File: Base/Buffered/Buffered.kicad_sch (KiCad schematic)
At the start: 17 parts, among them J1 Barrel_Jack_Switch, J2 Conn_01x04_Pin, J3 Conn_01x04_Pin, J4 AudioJack2_Ground, J5 AudioJack2_Ground, Q2 40V, SW1 SW_Push

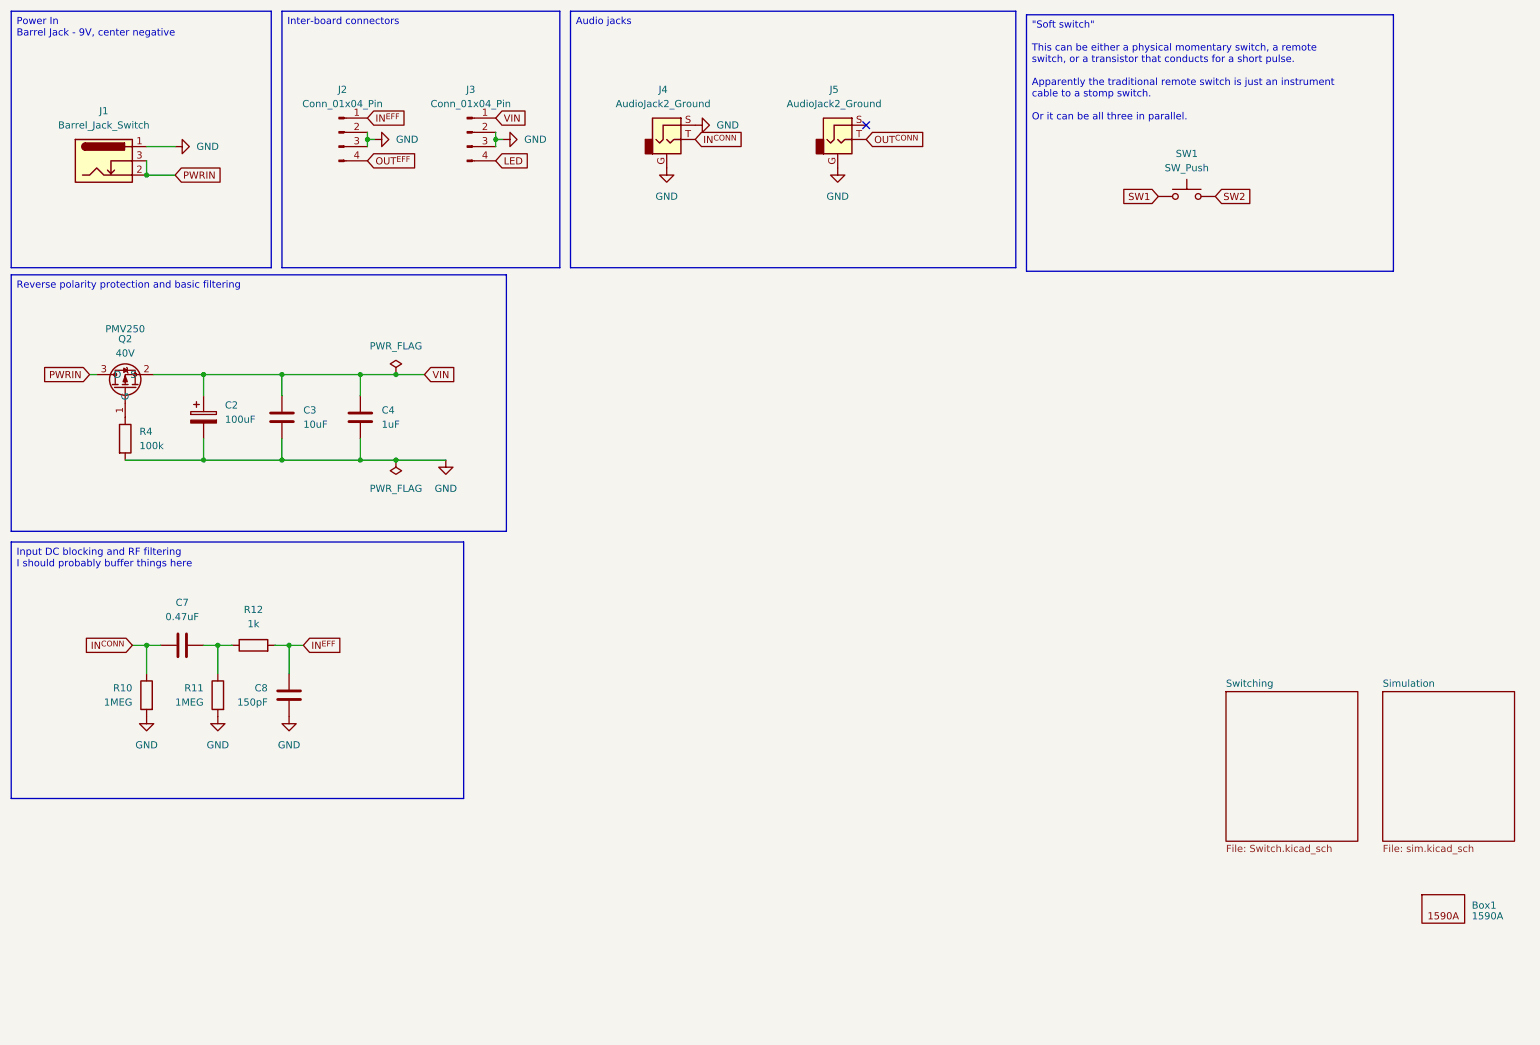
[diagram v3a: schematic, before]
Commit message: Add negative power rail to the buffered base design
The negative voltage isn't actually _used_ anywhere yet, but this is
prep-work for making that buffered base board do the long promised
buffering, as I'm currently leaning towards opamps.

The LT3462A is very easy to use, but in a probably completely misguided
attempt at keeping any stray ground return currents on the power supply
side, I added a ground plane keepout.  No isolation, but an attempt to
at least make the easy path for any return currents to stay in that
"power supply area" and hopefully not show up around the analog parts.

Somebody who knows what they are about would probably tell me I'm just
making things worse.  But I'm a sw engineer, so pretty much by
definition I don't know anybody who knows what they are doing.

Signed-off-by: Linus Torvalds <torvalds@linux-foundation.org>
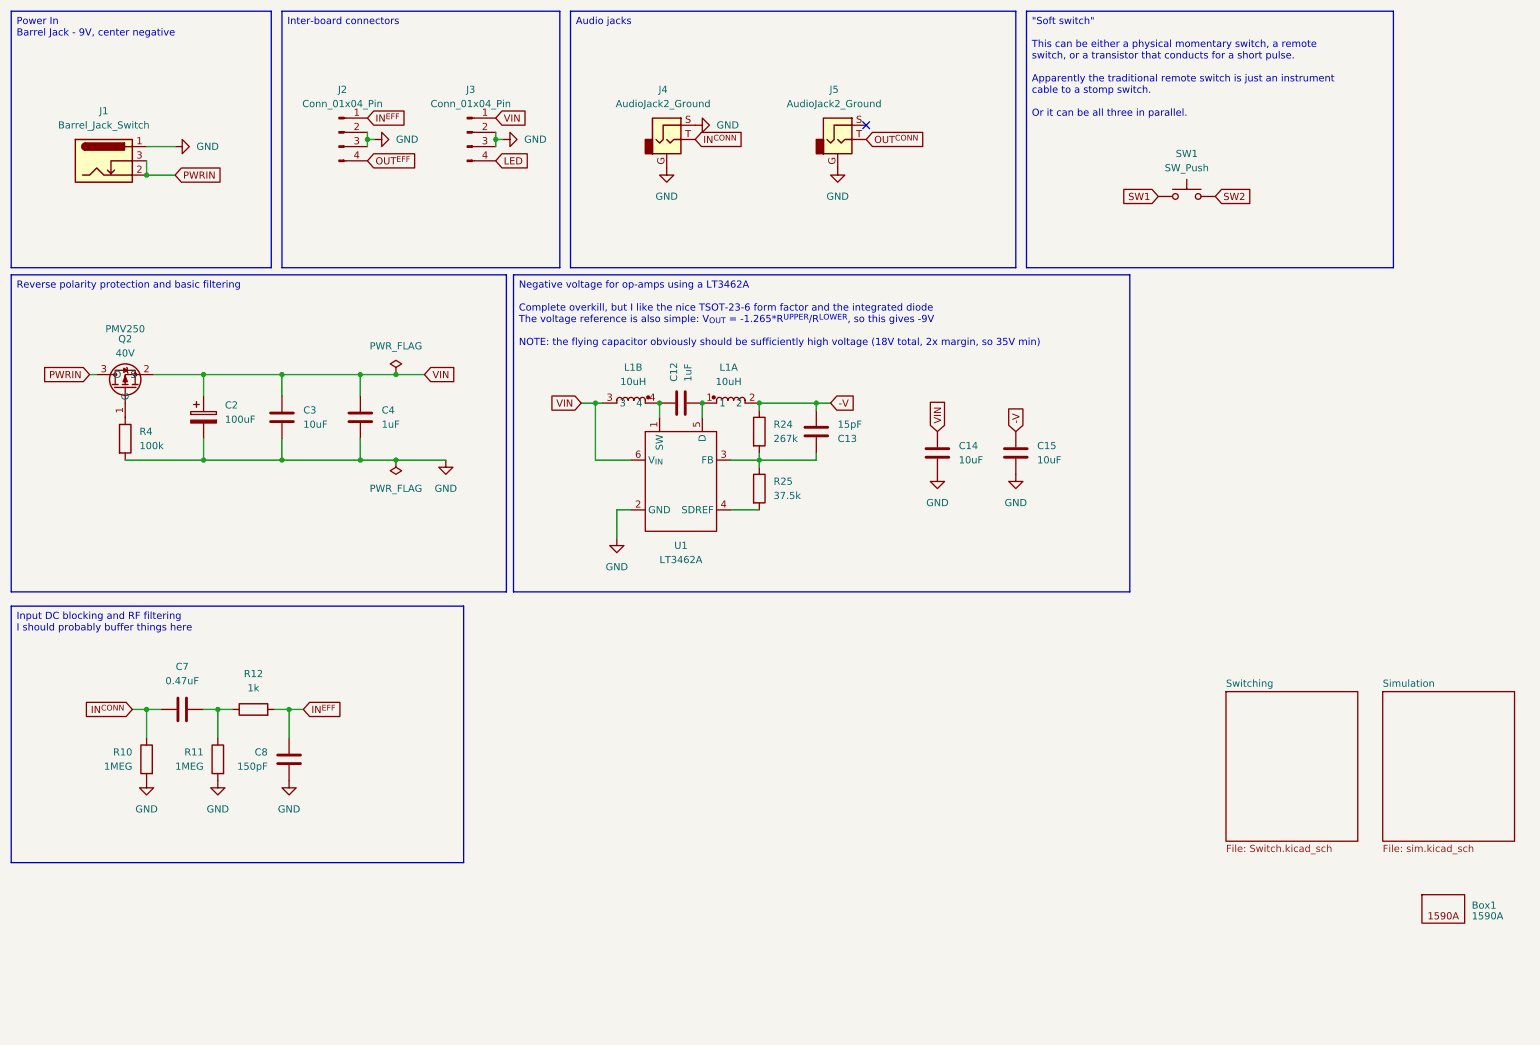
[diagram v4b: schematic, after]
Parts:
- added C12: 1uF, Capacitor_SMD:C_1206_3216Metric, symbol Device:C
- added C13: 15pF, Capacitor_SMD:C_0805_2012Metric, symbol Device:C
- added C14, C15: 10uF, Capacitor_SMD:C_1206_3216Metric, symbol Device:C
- added L1: 10uH, Mylib:LPD5030, symbol Mylib:LPD5030
- added R24: 267k, Resistor_SMD:R_0805_2012Metric, symbol Device:R
- added R25: 37.5k, Resistor_SMD:R_0805_2012Metric, symbol Device:R
- added U1: LT3462A, Package_TO_SOT_SMD:TSOT-23-6, symbol Mylib:LT3462AES6
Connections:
- net GND: now also C14.2, C15.2, U1.2 (GND)
- net VIN: now also C14.1, L1.3, U1.6 (V_{IN})
- new net: C12.2, L1.1, U1.5 (D)
- new net: C13.1, R24.2, R25.1, U1.3 (FB)
- new net: C12.1, L1.4, U1.1 (SW)
- new net: R25.2, U1.4 (SDREF)
- new net -V: C13.2, C15.1, L1.2, R24.1
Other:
- moved on the sheet: C7, C8, R10, R11, R12

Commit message: Buffered base: use negative rail for JFET switching
This _still_ doesn't do any actual buffering, but with the negative
rail, we now no longer need to rebase the signals to some mid-point
voltage, and we can just leave the signals ground-references and use the
negative rail for switching.

That streamlines the signal path, and will make it easier to just insert
an opamp or two in there too.  But I remain more interested in getting
the switching side sorted out properly, so that's the primary goal here.

This tweaks the push-on push-off circuit a bit too, since taht one now
needs to switch between positive and negative voltages rather than VIN
and ground.

Signed-off-by: Linus Torvalds <torvalds@linux-foundation.org>
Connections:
- net SW1: now also SW1.2; no longer SW1.1
- net SW2: now also SW1.1; no longer SW1.2
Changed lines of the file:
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@@
 		(lib_id "Switch:SW_Push")
 		(at 223.52 46.99 0)
+		(mirror y)
 		(unit 1)
 		(exclude_from_sim yes)
@@
 		(on_board yes)
 		(dnp no)
-		(fields_autoplaced yes)
 		(property "Reference" "SW1"
 			(at 223.52 39.37 0)

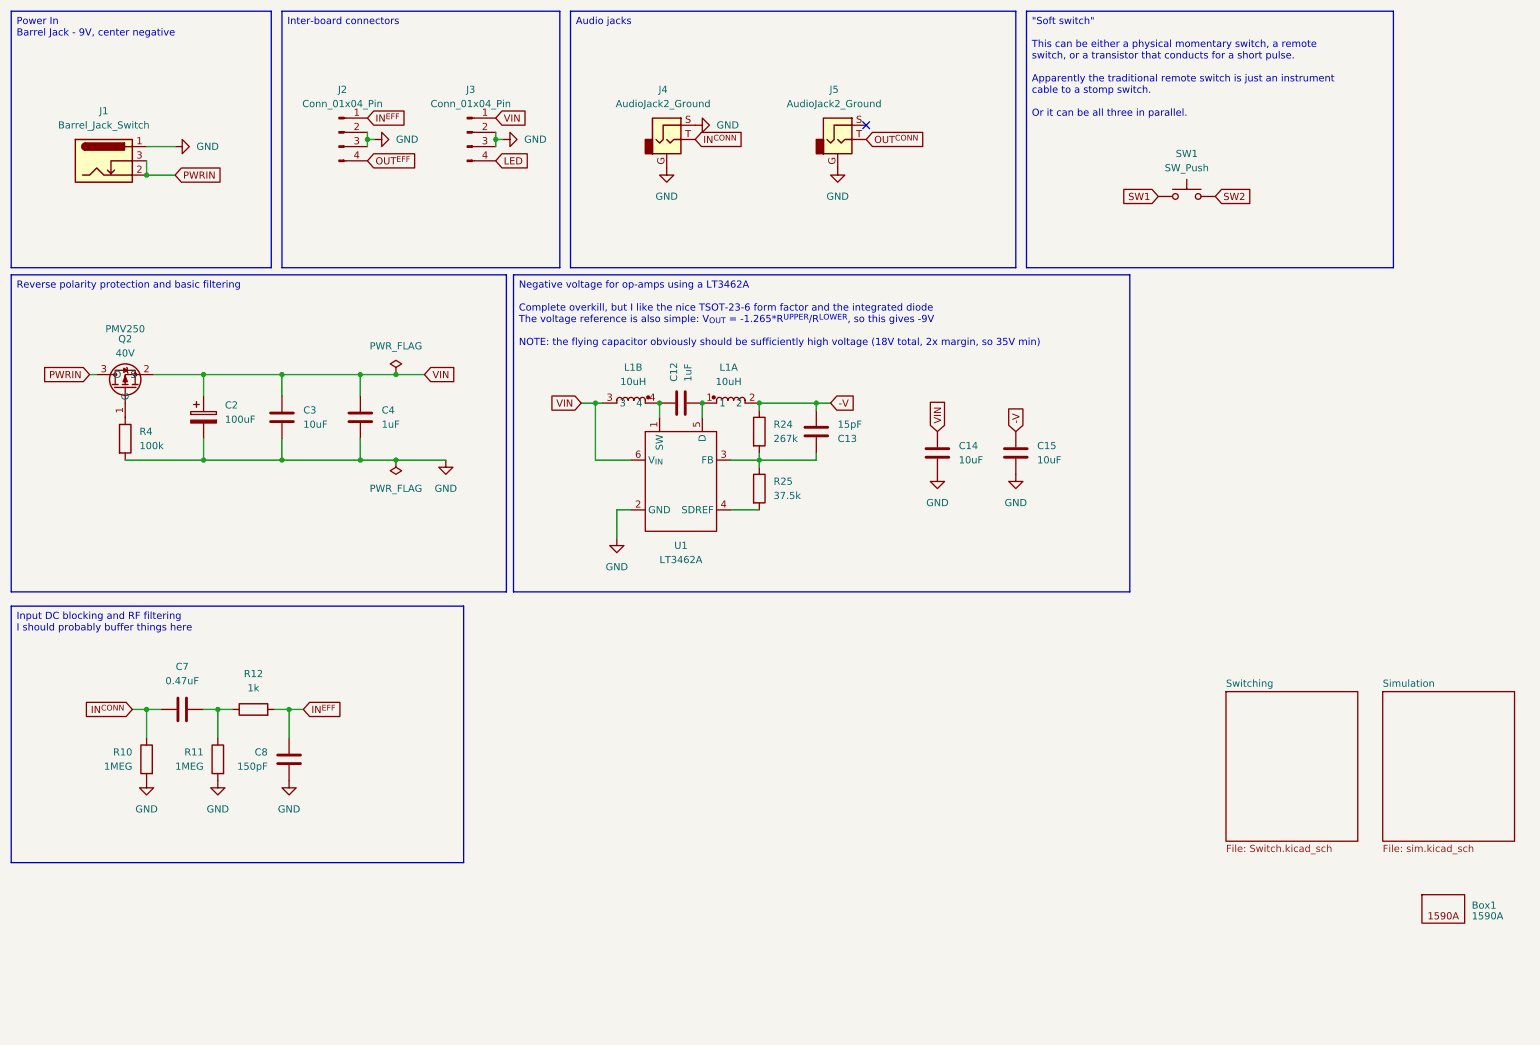
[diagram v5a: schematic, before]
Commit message: Update the buffered base board
The JFET switching worked fine, but since this all started as an
exercise in using MOSFETs, let's just go all in on that, and use the
MOSFETs for switching the signal too.

Due to the body diode, you need two MOSFETs in series for the signal
switching, so it's four MOSFETs instead of two JFETs, but despite that
the end result is actually simpler.  And those dual MOSFET things are
common and dirt cheap, unlike the special matched JFET package.

Since I can just continue to use the dual complementary MOSFETs, I can
use PMOS for one signal and NMOS for the other, and share all the gate
circuit.  Plus no need for a diode to protect the gate current messing
with the signal.

Also update the resistor value in the switching circuit and make the
time constant be 100ms.  That seems to make it more reliable in testing,
although I'm not convinced my testing with the original value was all
that great.  The soft-switch circuit does seem to work, though.

Also, since the LED pin on the board connectors has never been used,
let's just re-purpose that as a negative voltage pin for the effect
board.  If some effect board wants to touch the LED status, it might as
well just connect to the LED itself.  Having access to a dual voltage
rail would seem to be a lot more important.

Finally - and probably most importantly for actual sound and current
effects boards - add a low-pass filter on the voltage lines.  Because as
expected, the negative power supply did add a lot of noise to the VIN
line.

The base board itself doesn't actually care, but the effects boards do.

An actual LDO would be better, but I don't have any simple fixed ones in
my parts library (except for the 5V one, which seems a bit sad).
Current effects boards don't use a lot of current and only care about
the voltage being stable, so let's try this simple model.

Signed-off-by: Linus Torvalds <torvalds@linux-foundation.org>
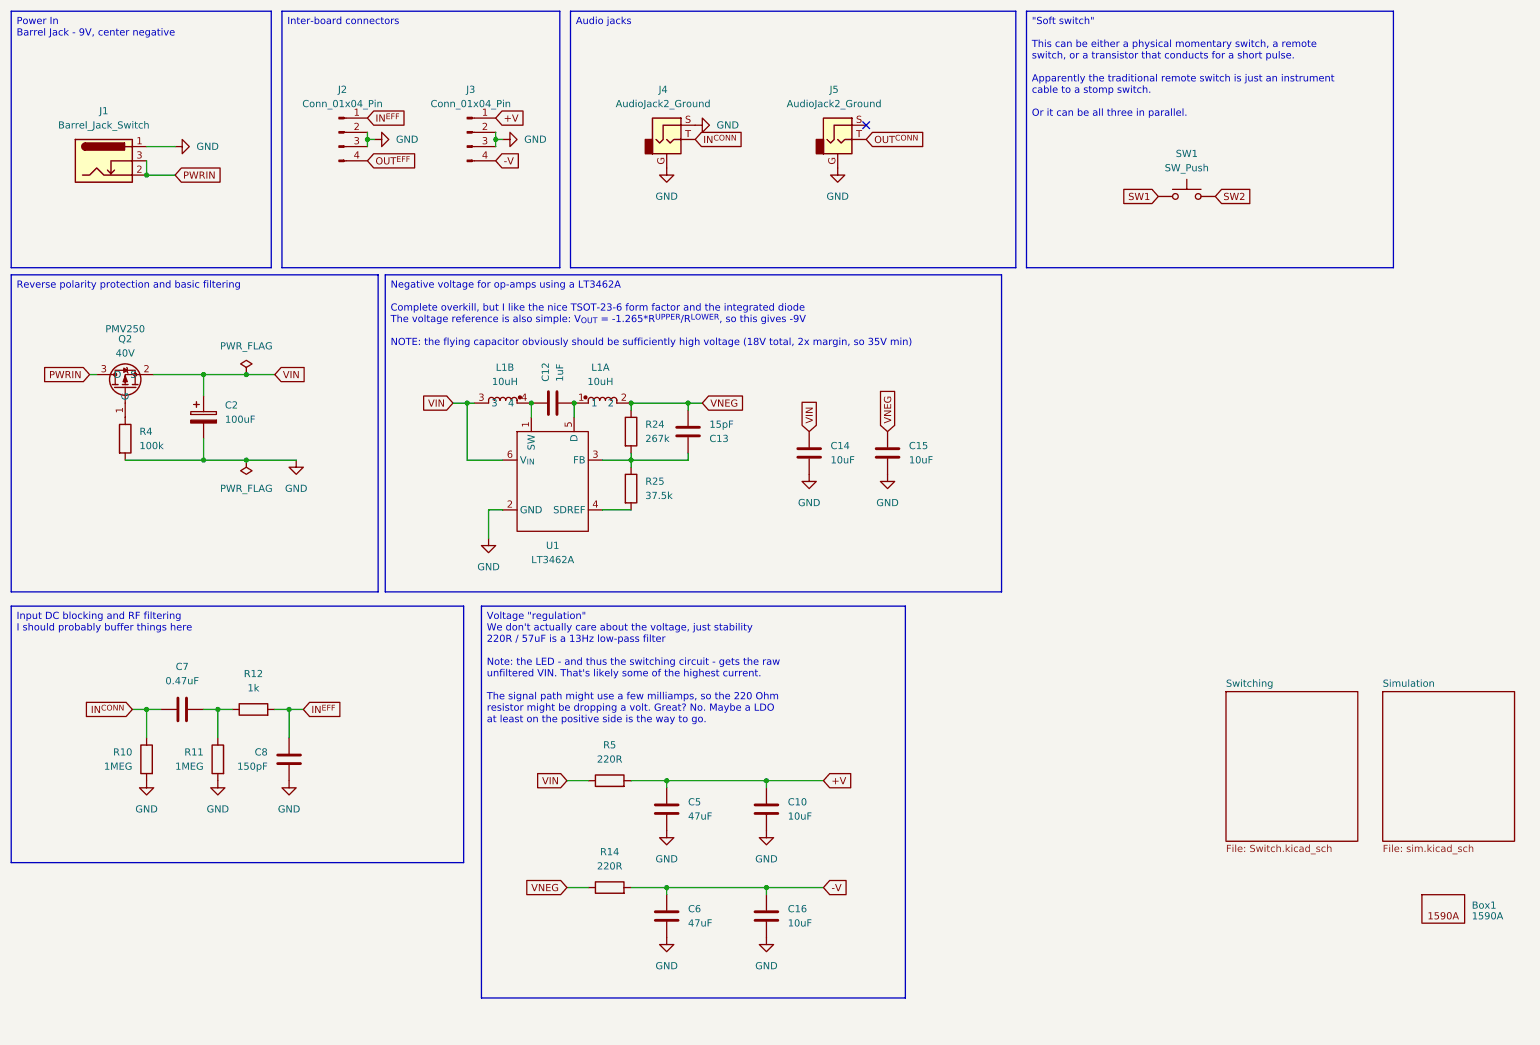
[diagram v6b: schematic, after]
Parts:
- removed C3: 10uF, Capacitor_SMD:C_1206_3216Metric, symbol Device:C
- removed C4: 1uF, Capacitor_SMD:C_1206_3216Metric, symbol Device:C
- added C10, C16: 10uF, Capacitor_SMD:C_1206_3216Metric, symbol Device:C
- added C5, C6: 47uF, Capacitor_SMD:C_1206_3216Metric, symbol Device:C
- added R14, R5: 220R, Resistor_SMD:R_0805_2012Metric, symbol Device:R
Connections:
- net LED is gone; now on net -V: J3.4 (Pin_4)
- net -V: now also C16.1, C6.1, R14.2; no longer C13.2, C15.1, L1.2, R24.1
- net GND: now also C10.2, C16.2, C5.2, C6.2
- net VIN: now also R5.1; no longer J3.1 (Pin_1)
- new net +V: C10.1, C5.1, J3.1 (Pin_1), R5.2
- new net VNEG: C13.2, C15.1, L1.2, R14.1, R24.1
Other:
- moved on the sheet: C12, C13, C14, C15, L1A, L1B, R24, R25, U1
